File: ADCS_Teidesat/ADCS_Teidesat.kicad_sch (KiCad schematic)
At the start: 27 parts, among them U1 MAX2659ELT+T, U2 L86-M33, U3 LSM6DSV16XTR, U4 LIS2MDLTR, U5 TMS5703137DPGEQQ1, Y1 ATX-H13-F-16.000MHz-G100-T

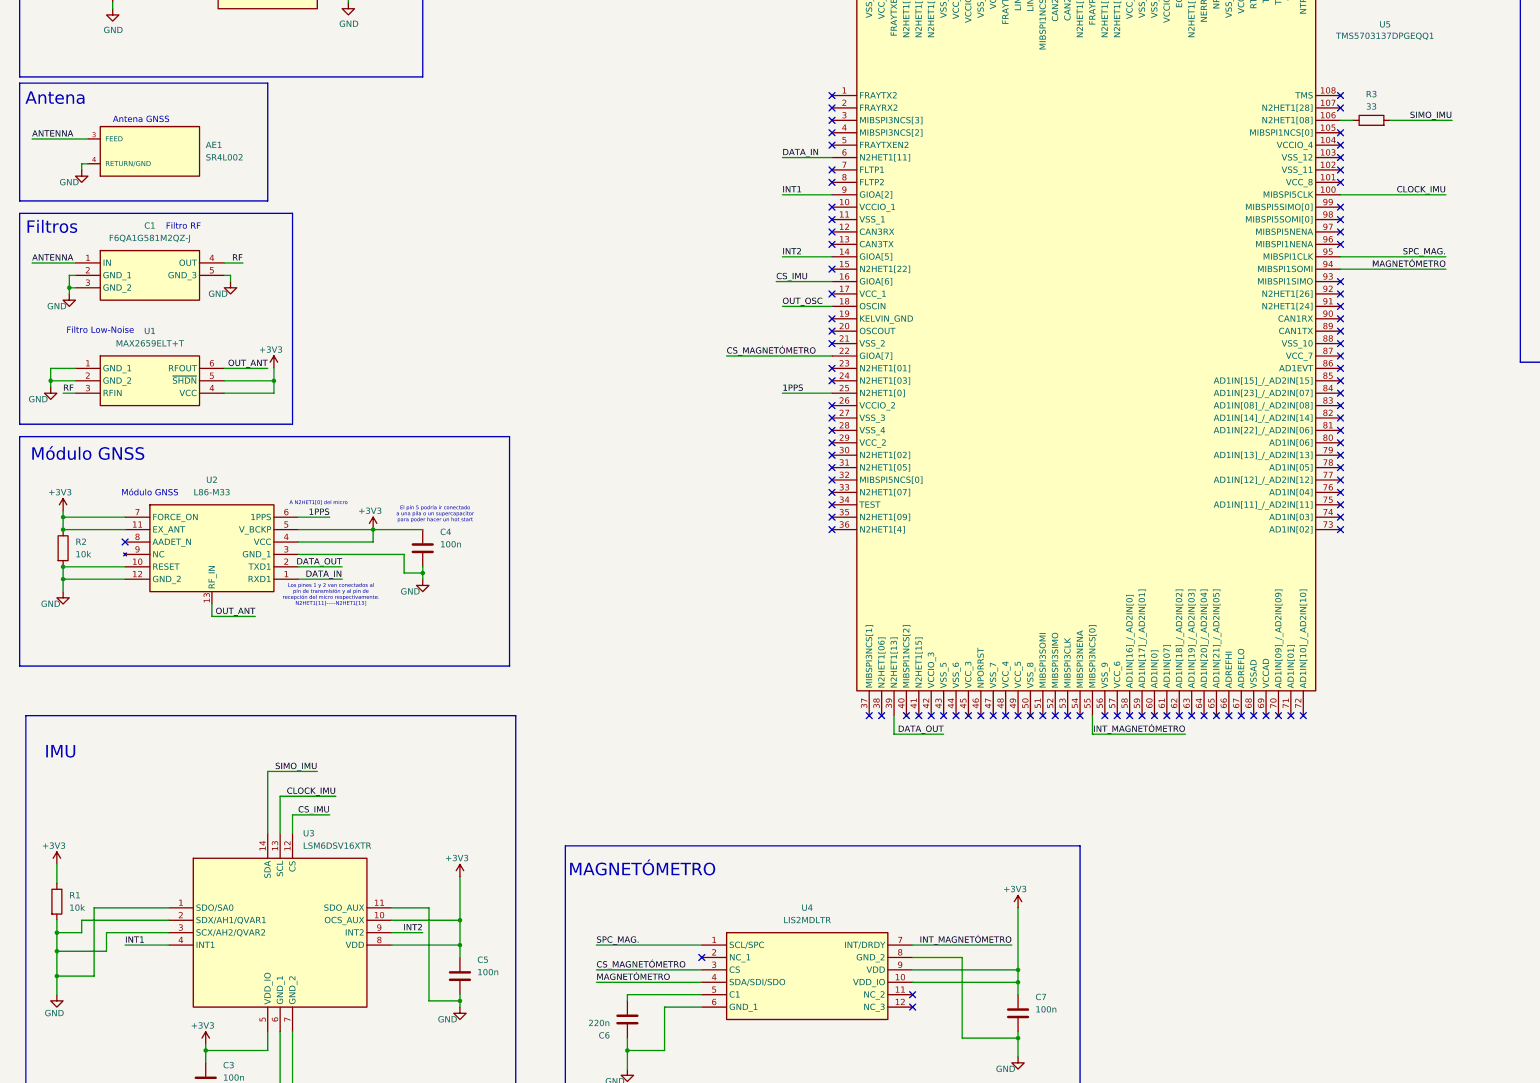
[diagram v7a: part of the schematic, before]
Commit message: Plano GND y Plano 3V3
He modificado la PCB de dos capas a cuatro capas. Con esto, hemos conseguido una capa  extra de GND y he añadido el plano de potencia.
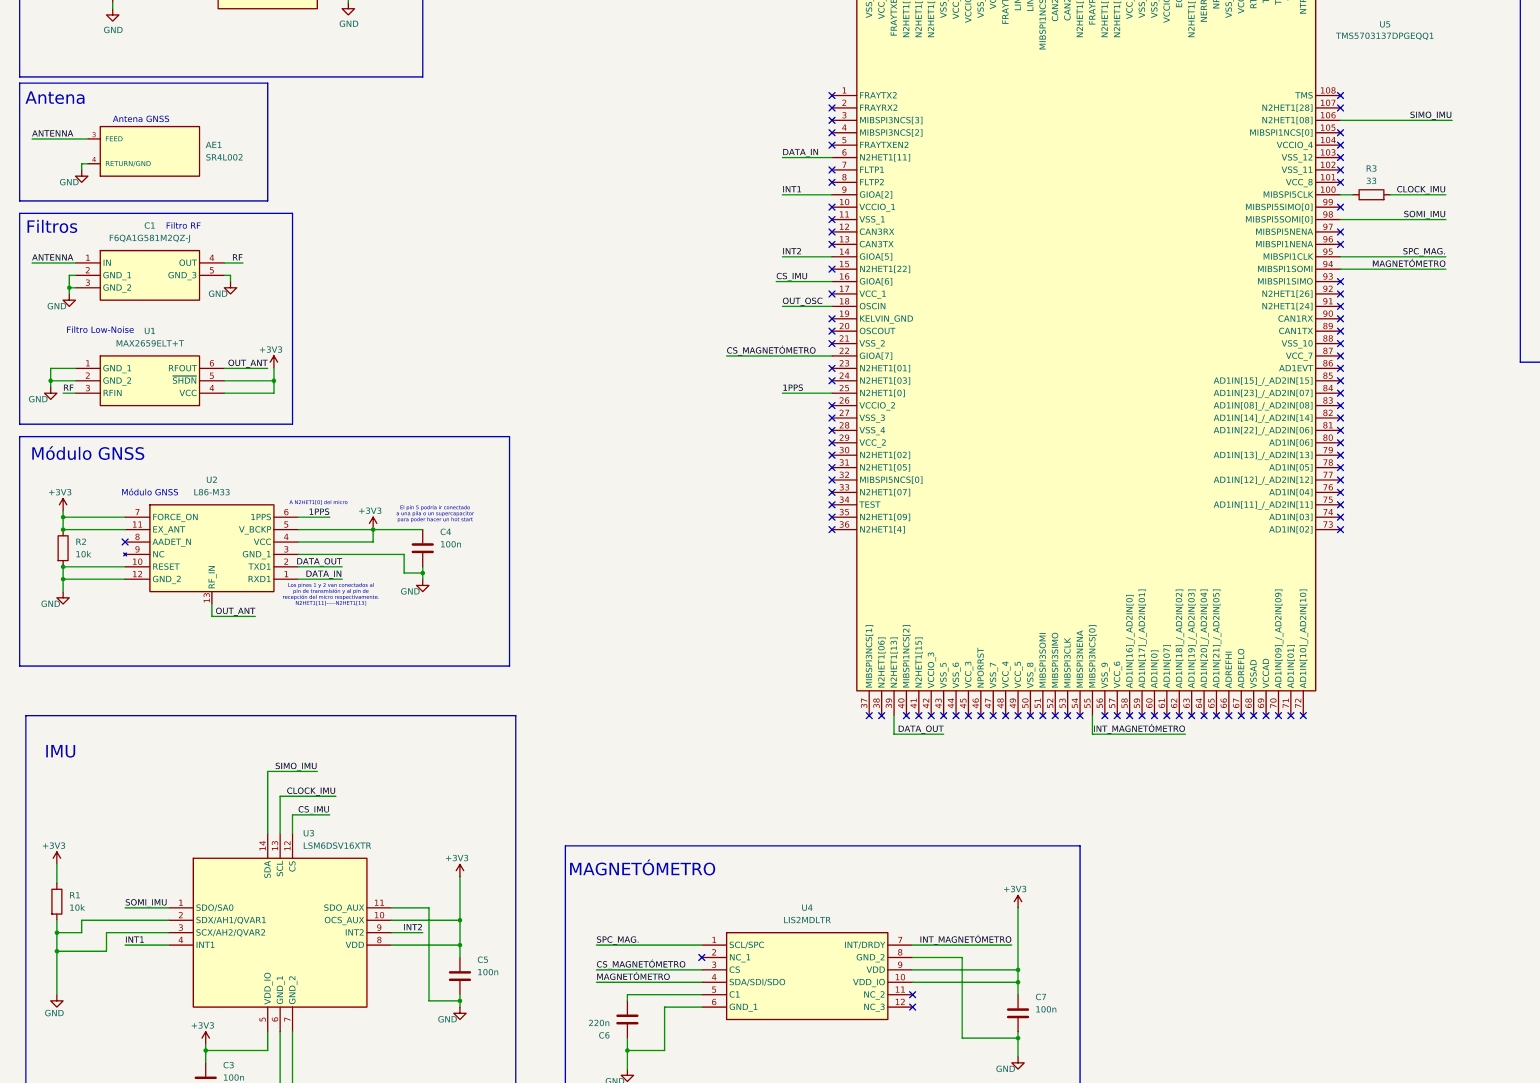
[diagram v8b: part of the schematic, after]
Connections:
- net CLOCK_IMU: now also R3.2; no longer U5.100 (MIBSPI5CLK)
- net GND: no longer U3.1 (SDO/SA0)
- net SIMO_IMU: now also U5.106 (N2HET1[08]); no longer R3.2
- net at R3.1: now also U5.100 (MIBSPI5CLK); no longer U5.106 (N2HET1[08])
- net SOMI_IMU: now reaches U5.98 (MIBSPI5SOMI[0])
- net SOMI_IMU: now also U3.1 (SDO/SA0)
- no-connect marks 239 -> 238
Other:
- moved on the sheet: R3
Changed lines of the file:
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@@
 	)
 	(junction
-		(at 20.32 238.76)
-		(diameter 0)
-		(color 0 0 0 0)
-	)
-	(junction
 		(at 20.32 229.87)
 		(diameter 0)
@@
 	)
 	(no_connect
-		(at 283.21 83.82)
-	)
-	(no_connect
 		(at 378.46 74.93)
 	)
@@
 	(wire
 		(pts
-			(xy 102.87 232.41) (xy 102.87 234.95)
+			(xy 34.29 224.79) (xy 43.18 224.79)
 		)
 		(stroke
@@
 	(wire
 		(pts
-			(xy 44.45 35.56) (xy 48.26 35.56)
+			(xy 102.87 232.41) (xy 102.87 234.95)
 		)
 		(stroke
@@
 	(wire
 		(pts
-			(xy 69.85 144.78) (xy 76.2 144.78)
+			(xy 44.45 35.56) (xy 48.26 35.56)
 		)
 		(stroke
@@
 	(wire
 		(pts
-			(xy 283.21 78.74) (xy 304.8 78.74)
+			(xy 69.85 144.78) (xy 76.2 144.78)
 		)
 		(stroke
@@
 	(wire
 		(pts
-			(xy 195.58 234.95) (xy 205.74 234.95)
+			(xy 283.21 63.5) (xy 306.07 63.5)
 		)
 		(stroke
@@
 	(wire
 		(pts
-			(xy 78.74 35.56) (xy 88.9 35.56)
+			(xy 195.58 234.95) (xy 205.74 234.95)
 		)
 		(stroke
@@
 	(wire
 		(pts
-			(xy 64.77 119.38) (xy 54.61 119.38)
+			(xy 78.74 35.56) (xy 88.9 35.56)
 		)
 		(stroke
@@
 	(wire
 		(pts
-			(xy 24.13 116.84) (xy 19.05 116.84)
+			(xy 64.77 119.38) (xy 54.61 119.38)
 		)
 		(stroke
@@
 	(wire
 		(pts
-			(xy 195.58 240.03) (xy 217.17 240.03)
+			(xy 24.13 116.84) (xy 19.05 116.84)
 		)
 		(stroke
@@
 	(wire
 		(pts
-			(xy 152.4 240.03) (xy 130.81 240.03)
+			(xy 195.58 240.03) (xy 217.17 240.03)
 		)
 		(stroke
@@
 	(wire
 		(pts
-			(xy 27.94 238.76) (xy 20.32 238.76)
+			(xy 152.4 240.03) (xy 130.81 240.03)
 		)
 		(stroke
@@
 	(wire
 		(pts
-			(xy 283.21 63.5) (xy 285.75 63.5)
-		)
-		(stroke
-			(width 0)
-			(type default)
-		)
-	)
-	(wire
-		(pts
 			(xy 217.17 251.46) (xy 217.17 255.27)
 		)
@@
 	(wire
 		(pts
+			(xy 293.37 78.74) (xy 304.8 78.74)
+		)
+		(stroke
+			(width 0)
+			(type default)
+		)
+	)
+	(wire
+		(pts
 			(xy 22.86 97.79) (xy 22.86 99.06)
 		)
@@
 	(wire
 		(pts
+			(xy 283.21 78.74) (xy 285.75 78.74)
+		)
+		(stroke
+			(width 0)
+			(type default)
+		)
+	)
+	(wire
+		(pts
 			(xy 96.52 243.84) (xy 102.87 243.84)
 		)
@@
 	(wire
 		(pts
-			(xy 293.37 63.5) (xy 306.07 63.5)
-		)
-		(stroke
-			(width 0)
-			(type default)
-		)
-	)
-	(wire
-		(pts
 			(xy 102.87 218.44) (xy 102.87 227.33)
 		)
@@
 	(wire
 		(pts
-			(xy 27.94 224.79) (xy 27.94 238.76)
-		)
-		(stroke
-			(width 0)
-			(type default)
-		)
-	)
-	(wire
-		(pts
 			(xy 31.75 39.37) (xy 31.75 40.64)
 		)
@@
 	(wire
 		(pts
-			(xy 20.32 238.76) (xy 20.32 242.57)
+			(xy 20.32 233.68) (xy 20.32 242.57)
 		)
 		(stroke
@@
 	(wire
 		(pts
-			(xy 43.18 224.79) (xy 27.94 224.79)
+			(xy 283.21 83.82) (xy 304.8 83.82)
 		)
 		(stroke
@@
 	(wire
 		(pts
-			(xy 20.32 233.68) (xy 20.32 238.76)
-		)
-		(stroke
-			(width 0)
-			(type default)
-		)
-	)
-	(wire
-		(pts
 			(xy 95.25 154.94) (xy 95.25 156.21)
 		)
@@
 		)
 	)
+	(label "SOMI_IMU"
+		(at 304.8 83.82 180)
+		(effects
+			(font
+				(size 1.27 1.27)
+			)
+			(justify right bottom)
+		)
+	)
 	(label "INT_MAGNETÓMETRO"
 		(at 251.46 189.23 180)
@@
 		)
 	)
+	(label "SOMI_IMU"
+		(at 34.29 224.79 0)
+		(effects
+			(font
+				(size 1.27 1.27)
+			)
+			(justify left bottom)
+		)
+	)
 	(label "SIMO_IMU"
 		(at 306.07 63.5 180)
@@
 	(symbol
 		(lib_id "Device:R")
-		(at 289.56 63.5 90)
+		(at 289.56 78.74 90)
 		(unit 1)
 		(exclude_from_sim no)
@@
 		(dnp no)
 		(property "Reference" "R3"
-			(at 289.56 58.166 90)
+			(at 289.56 73.406 90)
 			(effects
 				(font
@@
 		)
 		(property "Value" "33"
-			(at 289.56 60.706 90)
+			(at 289.56 75.946 90)
 			(effects
 				(font
@@
 		)
 		(property "Footprint" "Resistor_SMD:R_0201_0603Metric"
-			(at 289.56 65.278 90)
+			(at 289.56 80.518 90)
 			(effects
 				(font
@@
 		)
 		(property "Datasheet" "~"
-			(at 289.56 63.5 0)
+			(at 289.56 78.74 0)
 			(effects
 				(font
@@
 		)
 		(property "Description" "Resistor"
-			(at 289.56 63.5 0)
+			(at 289.56 78.74 0)
 			(effects
 				(font
